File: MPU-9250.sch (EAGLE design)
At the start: 5 parts, among them U1 MPU-9250

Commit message: Combination of the two sensors
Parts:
- added C3: 100 nF, eagle-ltspice:CC4564
- added R3, R4, R5: 10K, SparkFun-Resistors:10KOHM-1/10W-1%(0603)0603
- added U$1: MS580602BA52-51'A', myLibrary:MS580602BA52-51'A'
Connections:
- removed net AUX_CL: U1.AUX_CL
- removed net AUX_DA: U1.AUX_DA
- new net CS: R3.1, U1.!CS
- net GND: now also C3.2, U$1.GND
- net SCL/SCLK: now also R5.2, U$1.SCL
- net SDA/SDI: now also R4.2, U$1.SDA
- net VDD: now also C3.1, R4.1, R5.1, U$1.VDD
- net VDDIO: now also R3.2
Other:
- note added: "VDD"
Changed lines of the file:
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@@
 <part name="U1" library="Testing" deviceset="MPU-9250" device=""/>
 <part name="GND1" library="SparkFun-Aesthetics" deviceset="GND" device=""/>
-<part name="SUPPLY1" library="SparkFun-Aesthetics" deviceset="VCC" device="" value="VDD"/>
+<part name="VDD" library="SparkFun-Aesthetics" deviceset="VCC" device="" value="3.3 V"/>
 <part name="C1" library="SparkFun-Capacitors" deviceset="0.1UF-25V(+80/-20%)(0603)" device="" value="0.1uF"/>
 <part name="C2" library="SparkFun-Capacitors" deviceset="0.1UF-25V(+80/-20%)(0603)" device="" value="0.1uF"/>
@@
 <part name="R2" library="SparkFun-Resistors" deviceset="10KOHM-1/10W-1%(0603)" device="0603" value="10K"/>
 <part name="GND4" library="SparkFun-Aesthetics" deviceset="GND" device=""/>
+<part name="R3" library="SparkFun-Resistors" deviceset="10KOHM-1/10W-1%(0603)" device="0603" value="10K"/>
+<part name="U$1" library="myLibrary" deviceset="MS580602BA52-51" device="'A'"/>
+<part name="C3" library="eagle-ltspice" deviceset="C" device="C4564" value="100 nF"/>
+<part name="GND5" library="supply1" deviceset="GND" device=""/>
+<part name="SUPPLY1" library="SparkFun-Aesthetics" deviceset="VDD" device="" value="3.3 V"/>
+<part name="R4" library="SparkFun-Resistors" deviceset="10KOHM-1/10W-1%(0603)" device="0603" value="10K"/>
+<part name="R5" library="SparkFun-Resistors" deviceset="10KOHM-1/10W-1%(0603)" device="0603" value="10K"/>
+<part name="SUPPLY2" library="SparkFun-Aesthetics" deviceset="VDD" device="" value="3.3 V"/>
 </parts>
 <sheets>
 <sheet>
 <plain>
+<text x="48.26" y="114.3" size="1.778" layer="95">VDD</text>
+<text x="58.42" y="71.12" size="1.778" layer="91">VDD</text>
+<text x="111.76" y="33.02" size="1.778" layer="91">VDD</text>
 </plain>
 <instances>
 <instance part="U1" gate="G$1" x="101.6" y="104.14"/>
 <instance part="GND1" gate="1" x="78.74" y="83.82"/>
-<instance part="SUPPLY1" gate="G$1" x="55.88" y="114.3"/>
+<instance part="VDD" gate="G$1" x="55.88" y="114.3"/>
 <instance part="C1" gate="G$1" x="76.2" y="93.98" rot="MR0"/>
 <instance part="C2" gate="G$1" x="55.88" y="104.14" rot="MR0"/>
@@
 <instance part="R2" gate="G$1" x="142.24" y="114.3" rot="R90"/>
 <instance part="GND4" gate="1" x="63.5" y="88.9"/>
+<instance part="R3" gate="G$1" x="152.4" y="114.3" rot="R90"/>
+<instance part="U$1" gate="G$1" x="101.6" y="66.04"/>
+<instance part="C3" gate="G$1" x="66.04" y="68.58"/>
+<instance part="GND5" gate="1" x="66.04" y="58.42"/>
+<instance part="SUPPLY1" gate="VDD" x="66.04" y="71.12"/>
+<instance part="R4" gate="G$1" x="121.92" y="50.8" rot="R90"/>
+<instance part="R5" gate="G$1" x="129.54" y="48.26" rot="R90"/>
+<instance part="SUPPLY2" gate="VDD" x="121.92" y="35.56" rot="R180"/>
 </instances>
 <busses>
@@
 <wire x1="63.5" y1="104.14" x2="63.5" y2="91.44" width="0.1524" layer="91"/>
 </segment>
+<segment>
+<pinref part="GND5" gate="1" pin="GND"/>
+<wire x1="66.04" y1="63.5" x2="66.04" y2="60.96" width="0.1524" layer="91"/>
+<pinref part="C3" gate="G$1" pin="2"/>
+<pinref part="U$1" gate="G$1" pin="GND"/>
+<wire x1="88.9" y1="60.96" x2="66.04" y2="60.96" width="0.1524" layer="91"/>
+<junction x="66.04" y="60.96"/>
+</segment>
 </net>
 <net name="VDD" class="0">
 <segment>
-<pinref part="SUPPLY1" gate="G$1" pin="VCC"/>
+<pinref part="VDD" gate="G$1" pin="VCC"/>
 <wire x1="55.88" y1="114.3" x2="55.88" y2="111.76" width="0.1524" layer="91"/>
 <pinref part="U1" gate="G$1" pin="VDD"/>
@@
 <junction x="55.88" y="111.76"/>
 </segment>
+<segment>
+<pinref part="C3" gate="G$1" pin="1"/>
+<pinref part="SUPPLY1" gate="VDD" pin="VDD"/>
+<pinref part="U$1" gate="G$1" pin="VDD"/>
+<wire x1="88.9" y1="71.12" x2="66.04" y2="71.12" width="0.1524" layer="91"/>
+<junction x="66.04" y="71.12"/>
+</segment>
+<segment>
+<pinref part="R4" gate="G$1" pin="1"/>
+<wire x1="121.92" y1="45.72" x2="121.92" y2="38.1" width="0.1524" layer="91"/>
+<pinref part="R5" gate="G$1" pin="1"/>
+<wire x1="121.92" y1="38.1" x2="121.92" y2="35.56" width="0.1524" layer="91"/>
+<wire x1="129.54" y1="43.18" x2="129.54" y2="38.1" width="0.1524" layer="91"/>
+<wire x1="129.54" y1="38.1" x2="121.92" y2="38.1" width="0.1524" layer="91"/>
+<junction x="121.92" y="38.1"/>
+<pinref part="SUPPLY2" gate="VDD" pin="VDD"/>
+</segment>
 </net>
 <net name="VDDIO" class="0">
-<segment>
-<pinref part="U1" gate="G$1" pin="VDDIO"/>
-<wire x1="83.82" y1="109.22" x2="81.28" y2="109.22" width="0.1524" layer="91"/>
-<label x="81.28" y="109.22" size="1.27" layer="95" rot="R180" xref="yes"/>
-</segment>
 <segment>
 <wire x1="134.62" y1="121.92" x2="132.08" y2="121.92" width="0.1524" layer="91"/>
@@
 <junction x="134.62" y="121.92"/>
 <label x="132.08" y="121.92" size="1.27" layer="95" font="vector" rot="R180" xref="yes"/>
+<pinref part="R3" gate="G$1" pin="2"/>
+<wire x1="142.24" y1="121.92" x2="152.4" y2="121.92" width="0.1524" layer="91"/>
+<wire x1="152.4" y1="121.92" x2="152.4" y2="119.38" width="0.1524" layer="91"/>
+<junction x="142.24" y="121.92"/>
+</segment>
+<segment>
+<pinref part="U1" gate="G$1" pin="VDDIO"/>
+<wire x1="83.82" y1="109.22" x2="81.28" y2="109.22" width="0.1524" layer="91"/>
+<label x="81.28" y="109.22" size="1.27" layer="95" rot="R180" xref="yes"/>
 </segment>
 </net>
@@
 </segment>
 </net>
-<net name="AUX_CL" class="0">
-<segment>
-<pinref part="U1" gate="G$1" pin="AUX_CL"/>
-<wire x1="119.38" y1="111.76" x2="121.92" y2="111.76" width="0.1524" layer="91"/>
-<label x="121.92" y="111.76" size="1.27" layer="95" xref="yes"/>
-</segment>
-</net>
-<net name="AUX_DA" class="0">
-<segment>
-<pinref part="U1" gate="G$1" pin="AUX_DA"/>
-<wire x1="119.38" y1="109.22" x2="121.92" y2="109.22" width="0.1524" layer="91"/>
-<label x="121.92" y="109.22" size="1.27" layer="95" xref="yes"/>
-</segment>
-</net>
 <net name="SCL/SCLK" class="0">
 <segment>
 <pinref part="U1" gate="G$1" pin="SCL/SCLK"/>
 <wire x1="119.38" y1="104.14" x2="142.24" y2="104.14" width="0.1524" layer="91"/>
-<label x="152.4" y="104.14" size="1.27" layer="95" xref="yes"/>
+<label x="142.24" y="50.8" size="1.27" layer="95" xref="yes"/>
 <pinref part="R2" gate="G$1" pin="1"/>
-<wire x1="142.24" y1="104.14" x2="152.4" y2="104.14" width="0.1524" layer="91"/>
+<wire x1="142.24" y1="104.14" x2="142.24" y2="60.96" width="0.1524" layer="91"/>
+<wire x1="142.24" y1="60.96" x2="142.24" y2="50.8" width="0.1524" layer="91"/>
 <wire x1="142.24" y1="104.14" x2="142.24" y2="109.22" width="0.1524" layer="91"/>
 <junction x="142.24" y="104.14"/>
+<pinref part="U$1" gate="G$1" pin="SCL"/>
+<wire x1="114.3" y1="60.96" x2="129.54" y2="60.96" width="0.1524" layer="91"/>
+<junction x="142.24" y="60.96"/>
+<pinref part="R5" gate="G$1" pin="2"/>
+<wire x1="129.54" y1="60.96" x2="142.24" y2="60.96" width="0.1524" layer="91"/>
+<wire x1="129.54" y1="53.34" x2="129.54" y2="60.96" width="0.1524" layer="91"/>
+<junction x="129.54" y="60.96"/>
 </segment>
 </net>
@@
 <pinref part="U1" gate="G$1" pin="SDA/SDI"/>
 <wire x1="119.38" y1="101.6" x2="134.62" y2="101.6" width="0.1524" layer="91"/>
-<label x="152.4" y="101.6" size="1.27" layer="95" xref="yes"/>
+<label x="134.62" y="48.26" size="1.27" layer="95" xref="yes"/>
 <pinref part="R1" gate="G$1" pin="1"/>
-<wire x1="134.62" y1="101.6" x2="152.4" y2="101.6" width="0.1524" layer="91"/>
+<wire x1="134.62" y1="101.6" x2="134.62" y2="68.58" width="0.1524" layer="91"/>
+<wire x1="134.62" y1="68.58" x2="134.62" y2="48.26" width="0.1524" layer="91"/>
 <wire x1="134.62" y1="101.6" x2="134.62" y2="109.22" width="0.1524" layer="91"/>
 <junction x="134.62" y="101.6"/>
-</segment>
-</net>
+<pinref part="U$1" gate="G$1" pin="SDA"/>
+<wire x1="114.3" y1="68.58" x2="121.92" y2="68.58" width="0.1524" layer="91"/>
+<junction x="134.62" y="68.58"/>
+<pinref part="R4" gate="G$1" pin="2"/>
+<wire x1="121.92" y1="68.58" x2="134.62" y2="68.58" width="0.1524" layer="91"/>
+<wire x1="121.92" y1="68.58" x2="121.92" y2="55.88" width="0.1524" layer="91"/>
+<junction x="121.92" y="68.58"/>
+</segment>
+</net>
+<net name="CS" class="0">
+<segment>
+<pinref part="U1" gate="G$1" pin="!CS"/>
+<wire x1="119.38" y1="106.68" x2="152.4" y2="106.68" width="0.1524" layer="91"/>
+<label x="154.94" y="106.68" size="1.778" layer="95" xref="yes"/>
+<pinref part="R3" gate="G$1" pin="1"/>
+<wire x1="152.4" y1="106.68" x2="154.94" y2="106.68" width="0.1524" layer="91"/>
+<wire x1="152.4" y1="109.22" x2="152.4" y2="106.68" width="0.1524" layer="91"/>
+<junction x="152.4" y="106.68"/>
+</segment>
+</net>

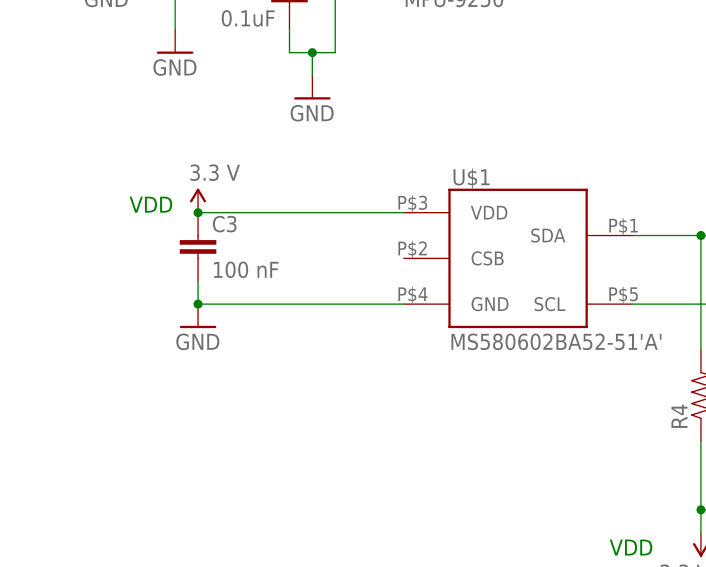
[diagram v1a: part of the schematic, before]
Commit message: Updated the final schematic
forgot to connect CSB to ground for the altimeter
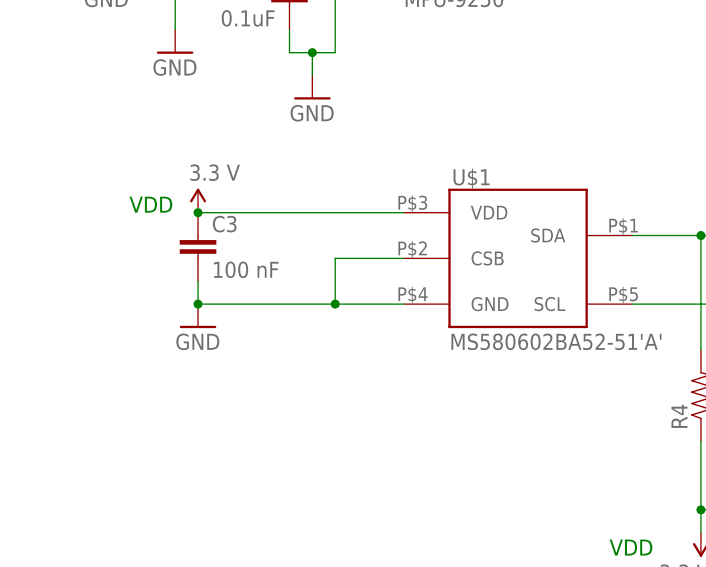
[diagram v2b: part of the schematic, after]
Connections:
- net GND: now also U$1.CSB
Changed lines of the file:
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@@
 <pinref part="C3" gate="G$1" pin="2"/>
 <pinref part="U$1" gate="G$1" pin="GND"/>
-<wire x1="88.9" y1="60.96" x2="66.04" y2="60.96" width="0.1524" layer="91"/>
+<wire x1="88.9" y1="60.96" x2="81.28" y2="60.96" width="0.1524" layer="91"/>
 <junction x="66.04" y="60.96"/>
+<pinref part="U$1" gate="G$1" pin="CSB"/>
+<wire x1="81.28" y1="60.96" x2="66.04" y2="60.96" width="0.1524" layer="91"/>
+<wire x1="88.9" y1="66.04" x2="81.28" y2="66.04" width="0.1524" layer="91"/>
+<wire x1="81.28" y1="66.04" x2="81.28" y2="60.96" width="0.1524" layer="91"/>
+<junction x="81.28" y="60.96"/>
 </segment>
 </net>
